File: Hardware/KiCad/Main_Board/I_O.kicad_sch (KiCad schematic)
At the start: 16 parts, among them J1 NC3FAAH-0, J2 NMJ4HFD2, J3 NMJ4HFD2, J4 57PC5F, J5 NMJ4HFD2, J6 NMJ4HFD2, U3 6N137

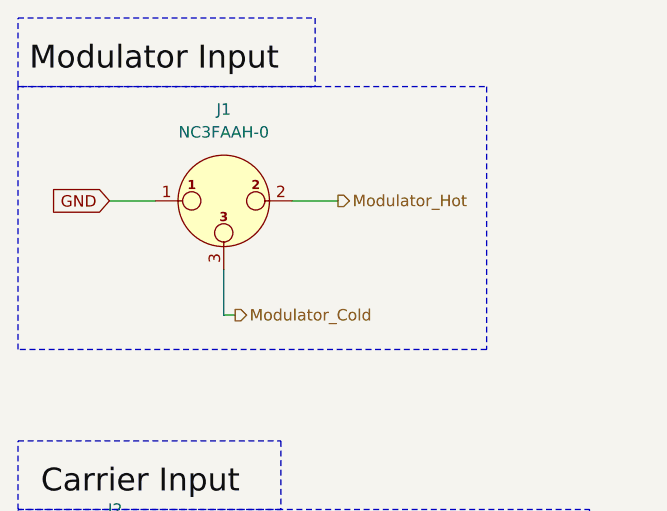
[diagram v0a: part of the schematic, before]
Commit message: Added PSU hierarchical inputs and outputs
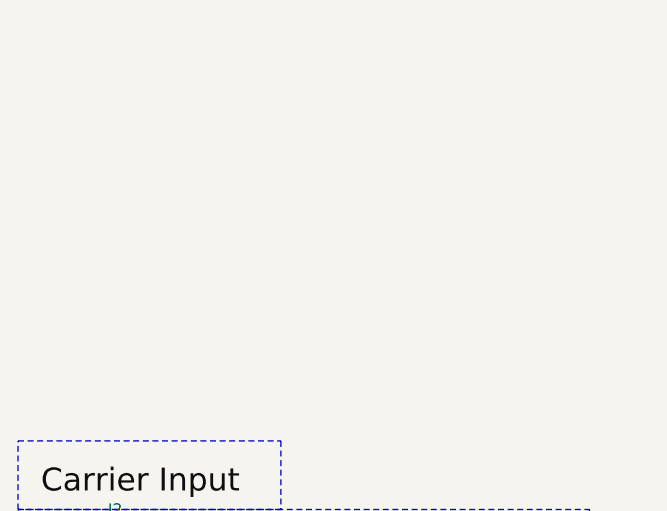
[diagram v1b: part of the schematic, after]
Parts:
- removed J1: NC3FAAH-0, Connector_Audio:Jack_XLR_Neutrik_NC3FAAH-0_Horizontal, symbol Connector_Audio:NC3FAAH-0
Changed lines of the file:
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@@
-	)
-	(rectangle
-		(start 22.86 21.59)
-		(end 55.88 29.21)
-		(stroke
-			(width 0)
-			(type dash)
-		)
-		(fill
-			(type none)
-		)
 	)
 	(rectangle
 		(start 22.86 68.58)
 		(end 52.07 76.2)
-		(stroke
-			(width 0)
-			(type dash)
-		)
-		(fill
-			(type none)
-		)
-	)
-	(rectangle
-		(start 22.86 29.21)
-		(end 74.93 58.42)
 		(stroke
 			(width 0)
@@
 	(wire
 		(pts
-			(xy 45.72 54.61) (xy 45.72 49.53)
-		)
-		(stroke
-			(width 0)
-			(type default)
-		)
-	)
-	(wire
-		(pts
 			(xy 102.87 148.59) (xy 106.68 148.59)
 		)
@@
 	(wire
 		(pts
-			(xy 46.99 54.61) (xy 45.72 54.61)
-		)
-		(stroke
-			(width 0)
-			(type default)
-		)
-	)
-	(wire
-		(pts
 			(xy 39.37 151.13) (xy 46.99 151.13)
 		)
@@
 	(wire
 		(pts
-			(xy 53.34 41.91) (xy 58.42 41.91)
-		)
-		(stroke
-			(width 0)
-			(type default)
-		)
-	)
-	(wire
-		(pts
 			(xy 128.27 151.13) (xy 132.08 151.13)
 		)
@@
 		(pts
 			(xy 41.91 158.75) (xy 41.91 166.37)
-		)
-		(stroke
-			(width 0)
-			(type default)
-		)
-	)
-	(wire
-		(pts
-			(xy 33.02 41.91) (xy 38.1 41.91)
 		)
 		(stroke
@@
 	(label "Carrier Input"
 		(at 25.4 74.93 0)
-		(effects
-			(font
-				(size 2.54 2.54)
-			)
-			(justify left bottom)
-		)
-	)
-	(label "Modulator Input"
-		(at 24.13 27.94 0)
 		(effects
 			(font
@@
 		)
 	)
-	(global_label "GND"
-		(shape input)
-		(at 33.02 41.91 180)
-		(fields_autoplaced yes)
-		(effects
-			(font
-				(size 1.27 1.27)
-			)
-			(justify right)
-		)
-		(property "Intersheetrefs" "${INTERSHEET_REFS}"
-			(at 26.1643 41.91 0)
-			(effects
-				(font
-					(size 1.27 1.27)
-				)
-				(justify right)
-				(hide yes)
-			)
-		)
-	)
 	(global_label "5V"
 		(shape input)
@@
 		)
 	)
-	(hierarchical_label "Modulator_Cold"
-		(shape output)
-		(at 46.99 54.61 0)
-		(effects
-			(font
-				(size 1.27 1.27)
-			)
-			(justify left)
-		)
-	)
 	(hierarchical_label "Midi_RX"
 		(shape output)
 		(at 152.4 151.13 0)
-		(effects
-			(font
-				(size 1.27 1.27)
-			)
-			(justify left)
-		)
-	)
-	(hierarchical_label "Modulator_Hot"
-		(shape output)
-		(at 58.42 41.91 0)
 		(effects
 			(font
@@
 					(unit 1)
 				)
-			)
-		)
-	)
-	(symbol
-		(lib_id "Connector_Audio:NC3FAAH-0")
-		(at 45.72 41.91 0)
-		(unit 1)
-		(exclude_from_sim no)
-		(in_bom yes)
-		(on_board yes)
-		(dnp no)
-		(fields_autoplaced yes)
-		(property "Reference" "J1"
-			(at 45.72 31.75 0)
-			(effects
-				(font
-					(size 1.27 1.27)
-				)
-			)
-		)
-		(property "Value" "NC3FAAH-0"
-			(at 45.72 34.29 0)
-			(effects
-				(font
-					(size 1.27 1.27)
-				)
-			)
-		)
-		(property "Footprint" "Connector_Audio:Jack_XLR_Neutrik_NC3FAAH-0_Horizontal"
-			(at 45.72 41.91 0)
-			(effects
-				(font
-					(size 1.27 1.27)
-				)
-				(hide yes)
-			)
-		)
-		(property "Datasheet" "https://www.neutrik.com/en/product/nc3faah-0"
-			(at 45.72 41.91 0)
-			(effects
-				(font
-					(size 1.27 1.27)
-				)
-				(hide yes)
-			)
-		)
-		(property "Description" "AA Series, 3 pole female XLR receptacle, grounding: without ground/shell contact, horizontal PCB mount, retention spring instead of latch"
-			(at 45.72 41.91 0)
-			(effects
-				(font
-					(size 1.27 1.27)
-				)
-				(hide yes)
-			)
-		)
-		(pin "3"
-		)
-		(pin "2"
-		)
-		(pin "1"
-		)
-		(instances
-			(project ""
-				(path "/e827c80a-ca8d-4d24-8db6-878b575a1aed/ae68f18c-05a9-496e-90b3-166bfef37cf7"
-					(reference "J1")
-					(unit 1)
-				)

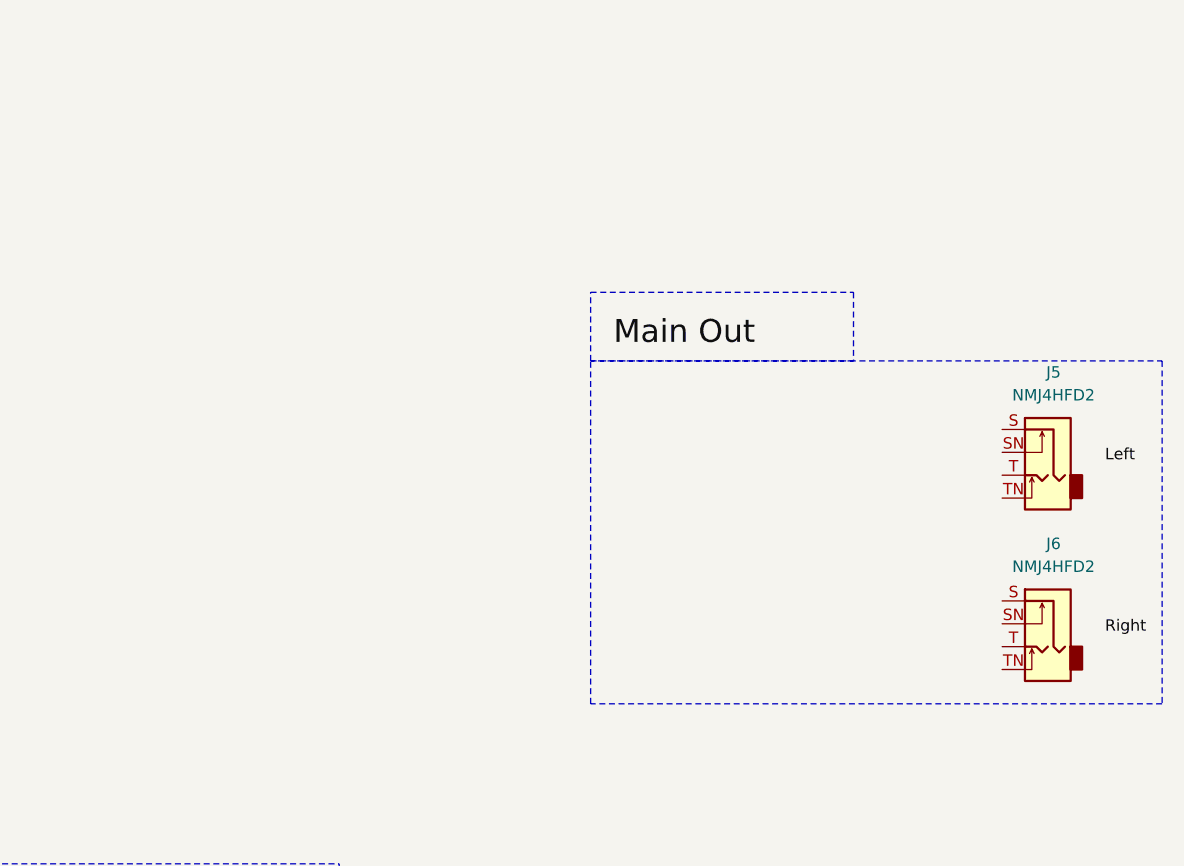
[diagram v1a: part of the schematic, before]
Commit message: Inserted SGTL5000 for the IO
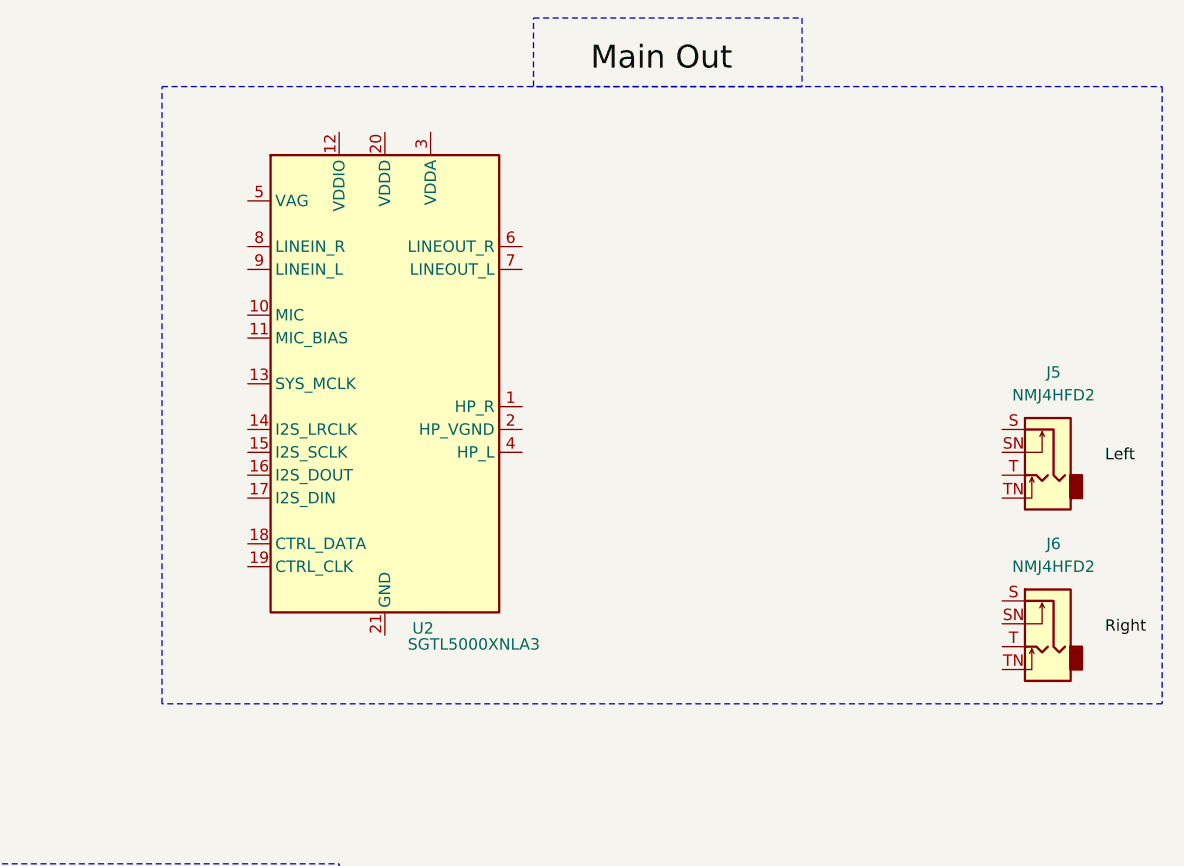
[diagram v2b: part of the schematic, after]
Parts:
- added U2: SGTL5000XNLA3, Package_DFN_QFN:QFN-20-1EP_3x3mm_P0.4mm_EP1.65x1.65mm, symbol Audio:SGTL5000XNLA3
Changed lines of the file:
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@@
 	)
 	(rectangle
-		(start 198.12 76.2)
+		(start 150.495 45.72)
 		(end 261.62 114.3)
 		(stroke
@@
 	)
 	(rectangle
-		(start 198.12 68.58)
-		(end 227.33 76.2)
+		(start 191.77 38.1)
+		(end 221.615 45.72)
 		(stroke
 			(width 0)
@@
 	)
 	(label "Main Out"
-		(at 200.66 74.93 0)
+		(at 198.12 44.45 0)
 		(effects
 			(font
@@
 					(unit 1)
 				)
+			)
+		)
+	)
+	(symbol
+		(lib_id "Audio:SGTL5000XNLA3")
+		(at 175.26 78.74 0)
+		(unit 1)
+		(exclude_from_sim no)
+		(in_bom yes)
+		(on_board yes)
+		(dnp no)
+		(property "Reference" "U2"
+			(at 178.308 105.918 0)
+			(effects
+				(font
+					(size 1.27 1.27)
+				)
+				(justify left)
+			)
+		)
+		(property "Value" "SGTL5000XNLA3"
+			(at 177.8 107.696 0)
+			(effects
+				(font
+					(size 1.27 1.27)
+				)
+				(justify left)
+			)
+		)
+		(property "Footprint" "Package_DFN_QFN:QFN-20-1EP_3x3mm_P0.4mm_EP1.65x1.65mm"
+			(at 175.26 78.74 0)
+			(effects
+				(font
+					(size 1.27 1.27)
+				)
+				(hide yes)
+			)
+		)
+		(property "Datasheet" "https://www.nxp.com/docs/en/data-sheet/SGTL5000.pdf"
+			(at 175.26 78.74 0)
+			(effects
+				(font
+					(size 1.27 1.27)
+				)
+				(hide yes)
+			)
+		)
+		(property "Description" "Low Power Stereo Codec with Headphone Amp, QFN-20"
+			(at 175.26 78.74 0)
+			(effects
+				(font
+					(size 1.27 1.27)
+				)
+				(hide yes)
+			)
+		)
+		(pin "17"
+		)
+		(pin "9"
+		)
+		(pin "5"
+		)
+		(pin "14"
+		)
+		(pin "8"
+		)
+		(pin "3"
+		)
+		(pin "12"
+		)
+		(pin "7"
+		)
+		(pin "11"
+		)
+		(pin "20"
+		)
+		(pin "21"
+		)
+		(pin "2"
+		)
+		(pin "19"
+		)
+		(pin "16"
+		)
+		(pin "15"
+		)
+		(pin "1"
+		)
+		(pin "18"
+		)
+		(pin "4"
+		)
+		(pin "6"
+		)
+		(pin "10"
+		)
+		(pin "13"
+		)
+		(instances
+			(project ""
+				(path "/e827c80a-ca8d-4d24-8db6-878b575a1aed/ae68f18c-05a9-496e-90b3-166bfef37cf7"
+					(reference "U2")
+					(unit 1)
+				)

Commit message: Changed outlining and combined input and main out
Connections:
- net 5V renamed +5V
- no-connect marks 5 -> 4
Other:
- moved on the sheet: J2, J3, J5, J6, U2
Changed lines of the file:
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@@
 	)
 	(rectangle
-		(start 22.86 76.2)
-		(end 86.36 114.3)
+		(start 88.9 24.13)
+		(end 118.745 31.75)
 		(stroke
 			(width 0)
@@
 	)
 	(rectangle
-		(start 150.495 45.72)
-		(end 261.62 114.3)
+		(start 26.67 45.72)
+		(end 55.245 85.09)
+		(stroke
+			(width 0)
+			(type dot)
+		)
+		(fill
+			(type none)
+		)
+	)
+	(rectangle
+		(start 164.465 49.53)
+		(end 193.04 91.44)
+		(stroke
+			(width 0)
+			(type dot)
+		)
+		(fill
+			(type none)
+		)
+	)
+	(rectangle
+		(start 19.05 31.75)
+		(end 198.12 118.745)
 		(stroke
 			(width 0)
@@
 		(start 22.86 124.46)
 		(end 35.56 132.08)
-		(stroke
-			(width 0)
-			(type dash)
-		)
-		(fill
-			(type none)
-		)
-	)
-	(rectangle
-		(start 191.77 38.1)
-		(end 221.615 45.72)
-		(stroke
-			(width 0)
-			(type dash)
-		)
-		(fill
-			(type none)
-		)
-	)
-	(rectangle
-		(start 22.86 68.58)
-		(end 52.07 76.2)
 		(stroke
 			(width 0)
@@
 	)
 	(no_connect
-		(at 121.92 148.59)
-	)
-	(no_connect
 		(at 40.64 143.51)
 	)
@@
 	)
 	(label "Right"
-		(at 255.27 106.68 0)
+		(at 190.5 81.28 180)
 		(effects
 			(font
 				(size 1.27 1.27)
 			)
-			(justify left bottom)
+			(justify right bottom)
 		)
 	)
 	(label "Left"
-		(at 255.27 87.63 0)
+		(at 189.23 62.23 180)
 		(effects
 			(font
 				(size 1.27 1.27)
 			)
+			(justify right bottom)
+		)
+	)
+	(label "Main Out"
+		(at 95.25 30.48 0)
+		(effects
+			(font
+				(size 2.54 2.54)
+			)
 			(justify left bottom)
 		)
 	)
 	(label "Right"
-		(at 22.86 106.68 0)
+		(at 29.21 76.2 0)
 		(effects
 			(font
@@
 	)
 	(label "Carrier Input"
-		(at 25.4 74.93 0)
+		(at 31.75 44.45 0)
 		(effects
 			(font
-				(size 2.54 2.54)
+				(face "KiCad Font")
+				(size 1.778 1.778)
 			)
 			(justify left bottom)
@@
 	)
 	(label "Main Out"
-		(at 198.12 44.45 0)
+		(at 185.42 48.26 180)
 		(effects
 			(font
-				(size 2.54 2.54)
-			)
-			(justify left bottom)
+				(size 1.778 1.778)
+			)
+			(justify right bottom)
 		)
 	)
 	(label "Left"
-		(at 22.86 87.63 0)
+		(at 30.48 58.42 0)
 		(effects
 			(font
@@
 		)
 	)
-	(global_label "5V"
-		(shape input)
-		(at 152.4 135.89 0)
-		(fields_autoplaced yes)
-		(effects
-			(font
-				(size 1.27 1.27)
-			)
-			(justify left)
-		)
-		(property "Intersheetrefs" "${INTERSHEET_REFS}"
-			(at 157.6833 135.89 0)
-			(effects
-				(font
-					(size 1.27 1.27)
-				)
-				(justify left)
-				(hide yes)
-			)
-		)
-	)
 	(global_label "GND"
 		(shape input)
@@
 				)
 				(justify right)
+				(hide yes)
+			)
+		)
+	)
+	(global_label "+5V"
+		(shape input)
+		(at 152.4 135.89 0)
+		(fields_autoplaced yes)
+		(effects
+			(font
+				(size 1.27 1.27)
+			)
+			(justify left)
+		)
+		(property "Intersheetrefs" "${INTERSHEET_REFS}"
+			(at 159.2557 135.89 0)
+			(effects
+				(font
+					(size 1.27 1.27)
+				)
+				(justify left)
 				(hide yes)
 			)
@@
 	(symbol
 		(lib_id "Connector_Audio:NMJ4HFD2")
-		(at 34.29 106.68 0)
+		(at 38.1 77.47 0)
 		(unit 1)
 		(exclude_from_sim no)
@@
 		(dnp no)
 		(property "Reference" "J3"
-			(at 33.655 95.25 0)
+			(at 38.1 66.548 0)
 			(effects
 				(font
@@
 		)
 		(property "Value" "NMJ4HFD2"
-			(at 33.655 97.79 0)
+			(at 38.1 69.088 0)
 			(effects
 				(font
@@
 		)
 		(property "Footprint" "Connector_Audio:Jack_6.35mm_Neutrik_NMJ4HFD2_Horizontal"
-			(at 34.29 101.6 0)
+			(at 38.1 72.39 0)
 			(effects
 				(font
@@
 		)
 		(property "Datasheet" "https://www.neutrik.com/en/product/nmj4hfd2"
-			(at 34.29 101.6 0)
+			(at 38.1 72.39 0)
 			(effects
 				(font
@@
 		)
 		(property "Description" "M Series, 6.35mm (1/4in) mono jack, switched, with full threaded nose and straight PCB pins"
-			(at 34.29 106.68 0)
+			(at 38.1 77.47 0)
 			(effects
 				(font
@@
 	(symbol
 		(lib_id "Connector_Audio:NMJ4HFD2")
-		(at 34.29 87.63 0)
+		(at 38.1 59.69 0)
 		(unit 1)
 		(exclude_from_sim no)
@@
 		(dnp no)
 		(property "Reference" "J2"
-			(at 33.655 76.2 0)
+			(at 38.735 49.022 0)
 			(effects
 				(font
@@
 		)
 		(property "Value" "NMJ4HFD2"
-			(at 33.655 78.74 0)
+			(at 38.1 51.308 0)
 			(effects
 				(font
@@
 		)
 		(property "Footprint" "Connector_Audio:Jack_6.35mm_Neutrik_NMJ4HFD2_Horizontal"
-			(at 34.29 82.55 0)
+			(at 38.1 54.61 0)
 			(effects
 				(font
@@
 		)
 		(property "Datasheet" "https://www.neutrik.com/en/product/nmj4hfd2"
-			(at 34.29 82.55 0)
+			(at 38.1 54.61 0)
 			(effects
 				(font
@@
 		)
 		(property "Description" "M Series, 6.35mm (1/4in) mono jack, switched, with full threaded nose and straight PCB pins"
-			(at 34.29 87.63 0)
+			(at 38.1 59.69 0)
 			(effects
 				(font
@@
 	(symbol
 		(lib_id "Connector_Audio:NMJ4HFD2")
-		(at 248.92 107.95 0)
+		(at 181.61 83.82 0)
 		(mirror y)
 		(unit 1)
@@
 		(dnp no)
 		(property "Reference" "J6"
-			(at 249.555 96.52 0)
+			(at 181.61 72.898 0)
 			(effects
 				(font
@@
 		)
 		(property "Value" "NMJ4HFD2"
-			(at 249.555 99.06 0)
+			(at 181.61 75.438 0)
 			(effects
 				(font
@@
 		)
 		(property "Footprint" "Connector_Audio:Jack_6.35mm_Neutrik_NMJ4HFD2_Horizontal"
-			(at 248.92 102.87 0)
+			(at 181.61 78.74 0)
 			(effects
 				(font
@@
 		)
 		(property "Datasheet" "https://www.neutrik.com/en/product/nmj4hfd2"
-			(at 248.92 102.87 0)
+			(at 181.61 78.74 0)
 			(effects
 				(font
@@
 		)
 		(property "Description" "M Series, 6.35mm (1/4in) mono jack, switched, with full threaded nose and straight PCB pins"
-			(at 248.92 107.95 0)
+			(at 181.61 83.82 0)
 			(effects
 				(font
@@
 	(symbol
 		(lib_id "Connector_Audio:NMJ4HFD2")
-		(at 248.92 88.9 0)
+		(at 181.61 64.77 0)
 		(mirror y)
 		(unit 1)
@@
 		(dnp no)
 		(property "Reference" "J5"
-			(at 249.555 77.47 0)
+			(at 181.61 53.848 0)
 			(effects
 				(font
@@
 		)
 		(property "Value" "NMJ4HFD2"
-			(at 249.555 80.01 0)
+			(at 181.61 56.388 0)
 			(effects
 				(font
@@
 		)
 		(property "Footprint" "Connector_Audio:Jack_6.35mm_Neutrik_NMJ4HFD2_Horizontal"
-			(at 248.92 83.82 0)
+			(at 181.61 59.69 0)
 			(effects
 				(font
@@
 		)
 		(property "Datasheet" "https://www.neutrik.com/en/product/nmj4hfd2"
-			(at 248.92 83.82 0)
+			(at 181.61 59.69 0)
 			(effects
 				(font
@@
 		)
 		(property "Description" "M Series, 6.35mm (1/4in) mono jack, switched, with full threaded nose and straight PCB pins"
-			(at 248.92 88.9 0)
+			(at 181.61 64.77 0)
 			(effects
 				(font
@@
 	(symbol
 		(lib_id "Audio:SGTL5000XNLA3")
-		(at 175.26 78.74 0)
+		(at 113.03 71.12 0)
 		(unit 1)
 		(exclude_from_sim no)
@@
 		(dnp no)
 		(property "Reference" "U2"
-			(at 178.308 105.918 0)
+			(at 116.078 98.298 0)
 			(effects
 				(font
@@
 		)
 		(property "Value" "SGTL5000XNLA3"
-			(at 177.8 107.696 0)
+			(at 115.57 100.076 0)
 			(effects
 				(font
@@
 		)
 		(property "Footprint" "Package_DFN_QFN:QFN-20-1EP_3x3mm_P0.4mm_EP1.65x1.65mm"
-			(at 175.26 78.74 0)
+			(at 113.03 71.12 0)
 			(effects
 				(font
@@
 		)
 		(property "Datasheet" "https://www.nxp.com/docs/en/data-sheet/SGTL5000.pdf"
-			(at 175.26 78.74 0)
+			(at 113.03 71.12 0)
 			(effects
 				(font
@@
 		)
 		(property "Description" "Low Power Stereo Codec with Headphone Amp, QFN-20"
-			(at 175.26 78.74 0)
-			(effects
-				(font
+			(at 113.03 71.12 0)
+			(effects
+				(font
